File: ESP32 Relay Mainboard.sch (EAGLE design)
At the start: 88 parts, among them J2 AUDIO_JACK_TRRSSMD_RA, J3 AUDIO_JACK_TRRSSMD_RA, J4 AUDIO_JACK_TRRSSMD_RA, J5 AUDIO_JACK_TRRSSMD_RA, J6 AUDIO_JACK_TRRSSMD_RA, K1 SRD-05VDC-SL-C, K2 SRD-05VDC-SL-C, K3 SRD-05VDC-SL-C, K4 SRD-05VDC-SL-C, K5 SRD-05VDC-SL-C, K6 SRD-05VDC-SL-C, U1 ESP32-S2-WROOM, U2 CP2104, U4 LM2576SX-5.0/NOPB

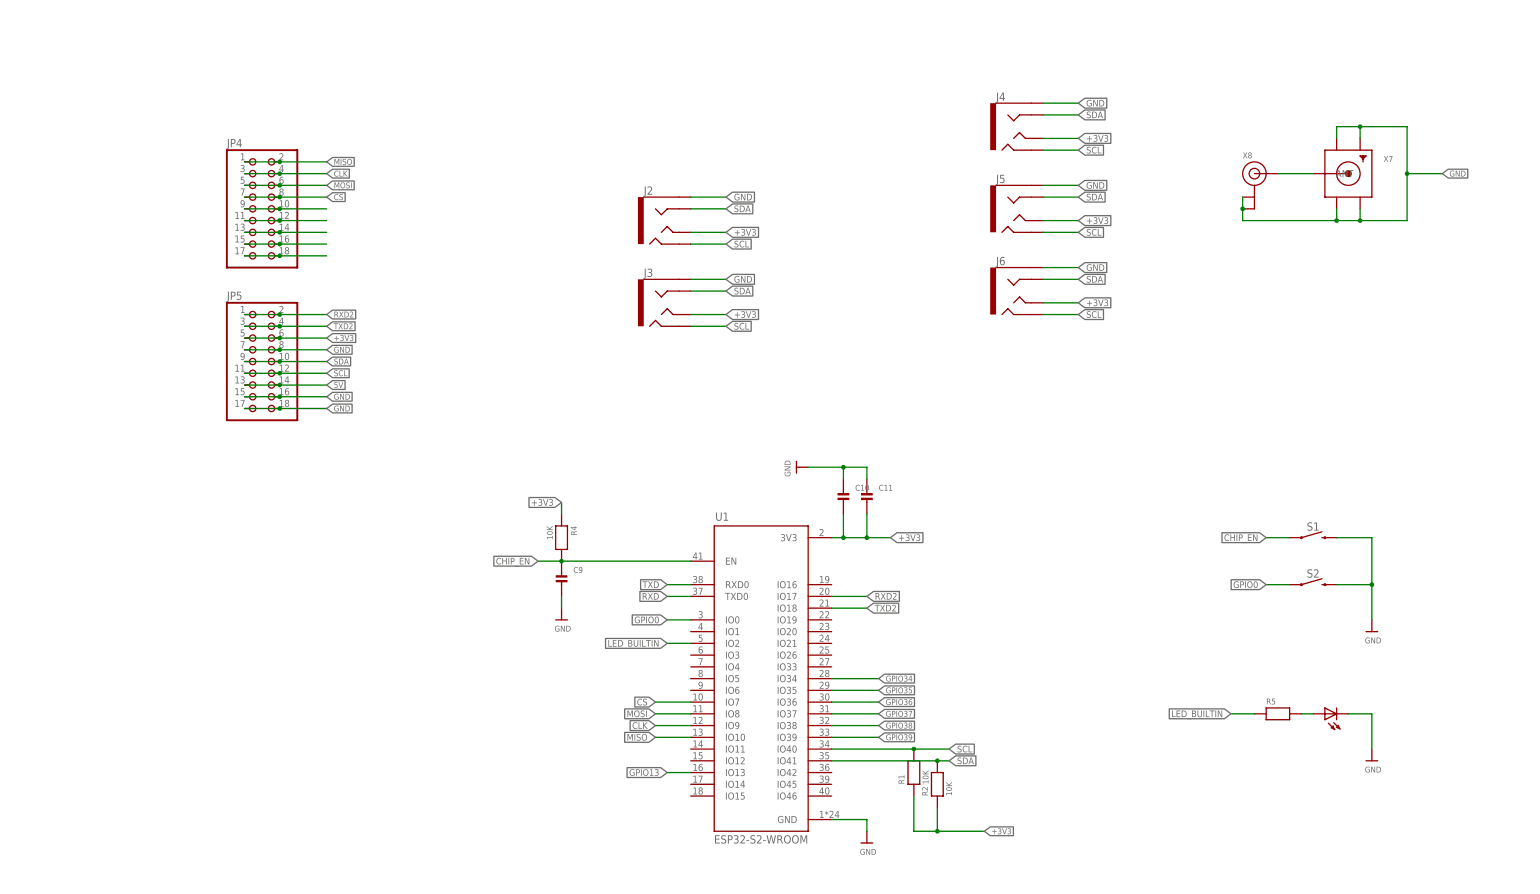
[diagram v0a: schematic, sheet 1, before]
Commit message: Add files via upload
Added second UART port. Added OTG usb. Removed CP2102. Added 6th jack connector. Added labels.
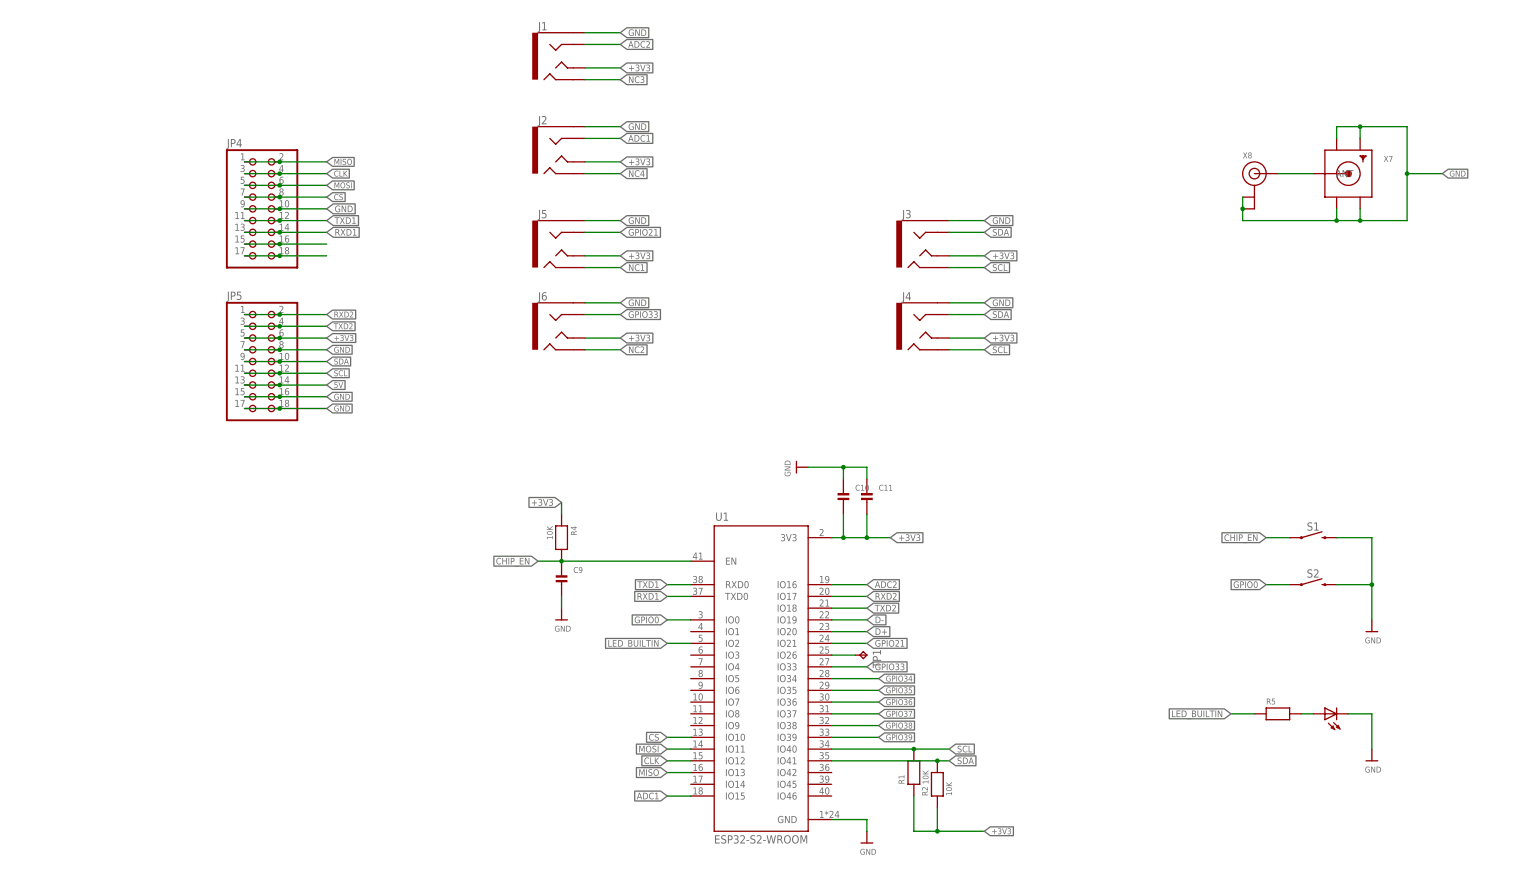
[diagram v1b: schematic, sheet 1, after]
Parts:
- removed C4: 4.7uF, SparkFun-Capacitors:22UF-0805-6.3V-20%
- removed C5: 0.1uF, SparkFun-Capacitors:22UF-0805-6.3V-20%
- removed U2: CP2104, microbuilder:CP2104
- added J1: AUDIO_JACK_TRRSSMD_RA, SparkFun-Connectors:AUDIO_JACK_TRRSSMD_RA
- added R3, R6: 5.1K, microbuilder:RESISTOR0603
- added TP1: TPTP20R, testpad:TPTP20R
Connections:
- removed net DTR: U2G$1.DTR
- removed net GPIO13: U1.IO13
- removed net N$167: JP4.10, JP4.9
- removed net N$168: JP4.11, JP4.12
- removed net N$170: JP4.13, JP4.14
- removed net RTS: U2G$1.RTS
- removed net RXD: U1.TXD0, U2G$1.RXD
- removed net TXD: U1.RXD0, U2G$1.TXD
- new net ADC1: J2.RING1, U1.IO15
- new net ADC2: J1.RING1, U1.IO16
- new net GPIO21: J5.RING1, U1.IO21
- new net GPIO33: J6.RING1, U1.IO33
- new net N$10: CONN1.CC1, R6.2
- new net N$17: TP1.TP, U1.IO26
- new net NC1: J5.RING2
- new net NC2: J6.RING2
- new net NC3: J1.RING2
- new net NC4: J2.RING2
- new net RXD1: JP4.13, JP4.14, U1.TXD0
- new net TXD1: JP4.11, JP4.12, U1.RXD0
- net +3V3: now also J1.TIP; no longer C5.1, U2G$1.REGIN, U2G$1.VDD, U2G$1.VIO
- net CLK: now also U1.IO12; no longer U1.IO9
- net CS: now also U1.IO10; no longer U1.IO7
- net D+: now also U1.IO20; no longer U2G$1.D+
- net D-: now also U1.IO19; no longer U2G$1.D-
- net GND: now also J1.EARTH, JP4.10, JP4.9, R3.1, R6.1; no longer C4.2, C5.2, U2G$1.GND, U2G$2.TP
- net MISO: now also U1.IO13; no longer U1.IO10
- net MOSI: now also U1.IO11; no longer U1.IO8
- net N$13: now also CONN1.CC2, R3.2; no longer C4.1, U2G$1.VPP
- net SCL: no longer J2.RING2, J5.RING2, J6.RING2
- net SDA: no longer J2.RING1, J5.RING1, J6.RING1
- net VBUS: no longer U2G$1.VBUS
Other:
- moved on the sheet: C1, D8, J2, J3, J4, J5, J6

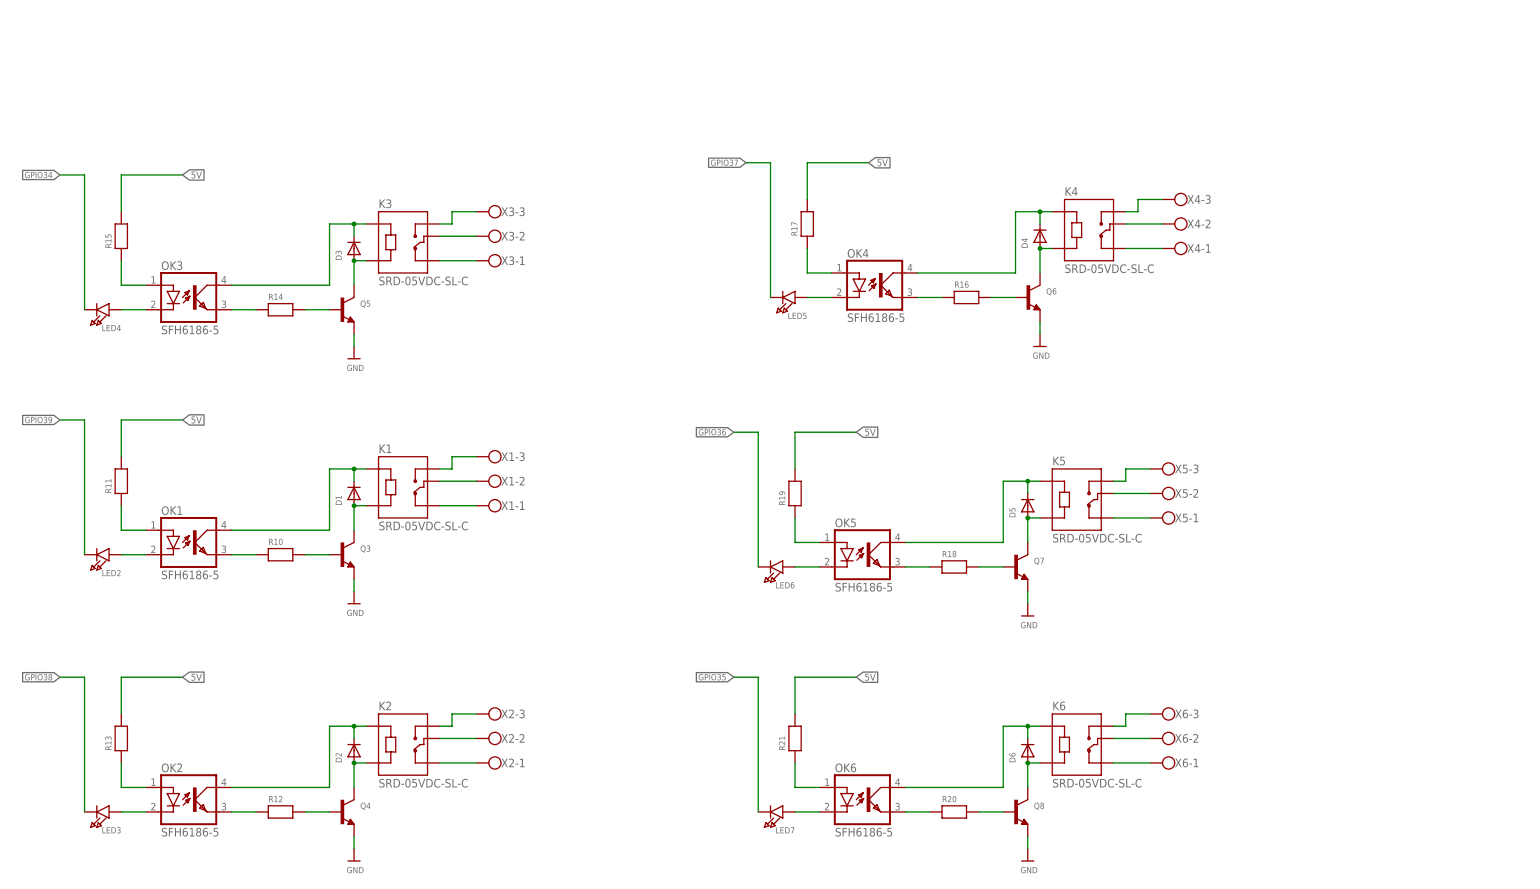
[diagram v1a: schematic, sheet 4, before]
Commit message: Updated the schematic with values
Added values to components (resistors and caps). Also added a description to some parts of the board.
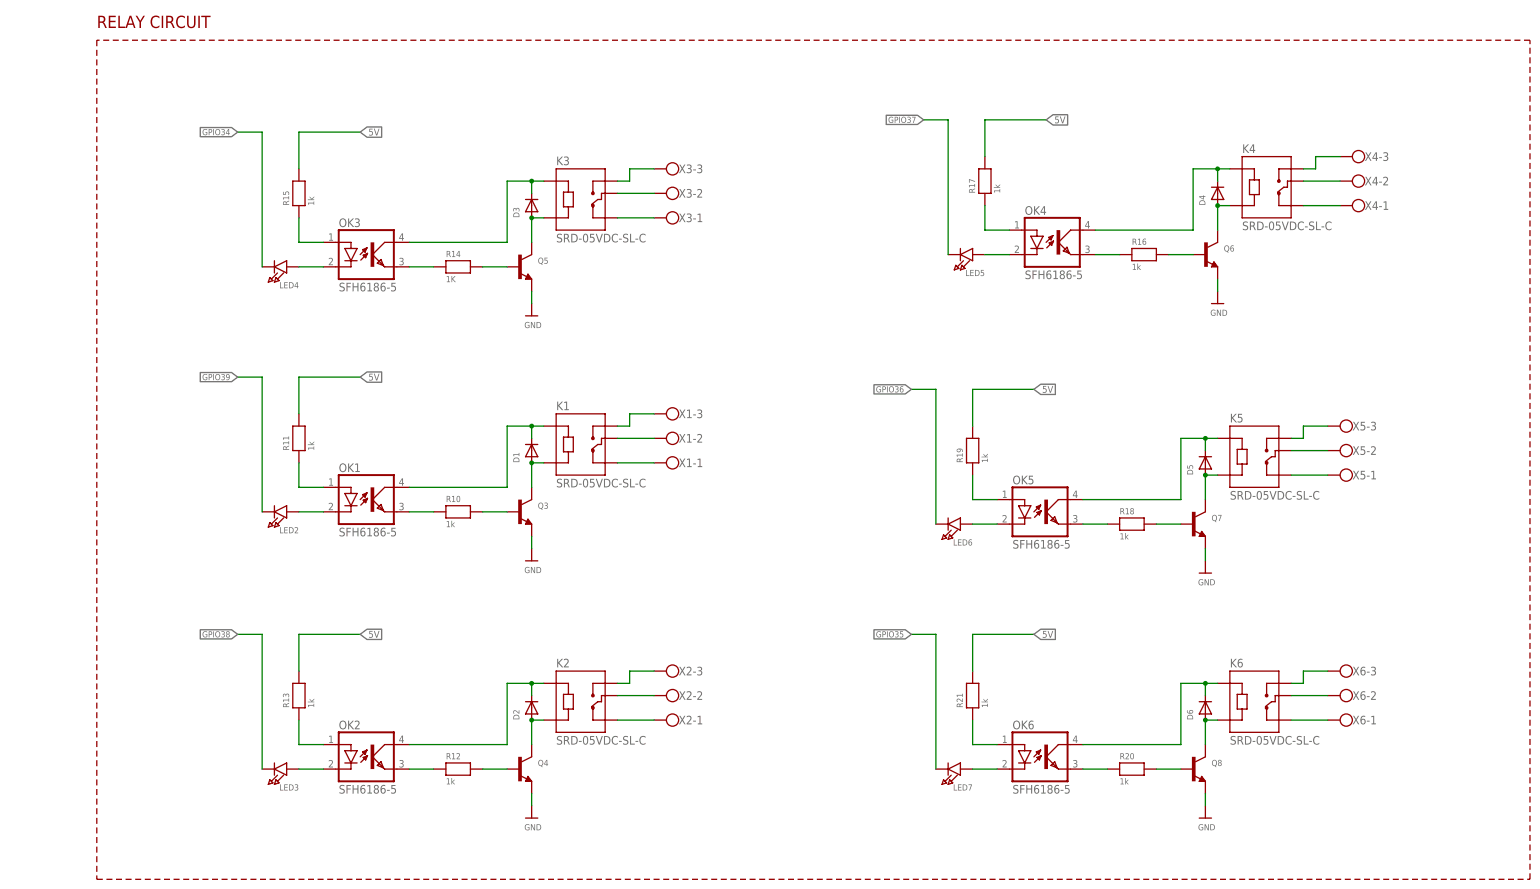
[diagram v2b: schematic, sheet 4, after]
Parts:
- C10, C9: value (none) -> 0.1uF
- C11: value (none) -> 0.1uf
- C2, C6: value (none) -> 10uF
- C3: value (none) -> 100uF
- R10, R11, R12, R13, R15, R16, R17, R18, R19, R20, R21: value (none) -> 1k
- R14, R22, R5: value (none) -> 1K
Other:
- note added: "50OHM IMPEDANCE TRACE & SMA"
- note added: "5V is directly connected to AMS1117-3.3 3.3V regulator 1A ouput"
- note added: "ANALOG JACK CONNECTORS"
- note added: "BUCK CONVERTER & REGULATOR"
- note added: "BUILTIN LED"
- note added: "Buck converter is LM2576, input is up tp 40V and output is 5V 3.5A"
- note added: "DIGITAL JACK CONNECTORS"
- note added: "ESP32-S2 MCU"
- note added: "FLASH & RESET"
- note added: "HEADER PINS"
- note added: "I2C JACK CONNECTORS"
- note added: "RELAY CIRCUIT"
- note added: "SHLD (USB-C shield pin) is left floating to avoid EMI"
- note added: "Two 5.1K resistors for USB-C connection detection."
- note added: "USB type C connector circuit with 500mA PTC fuse"
- note added: "USB-C CONNECTOR"
- note added: "reduce parasitic drain."
- note added: "to interfere in data lines. Added a 1uF capacitor to"
- moved on the sheet: C1, CONN1, D1, D2, D3, D4, D5, D6, D7, D8, F2, J1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

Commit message: Add files via upload
Removed optocouplers. added AZ1045 ESD protection array to D+ and D- lines
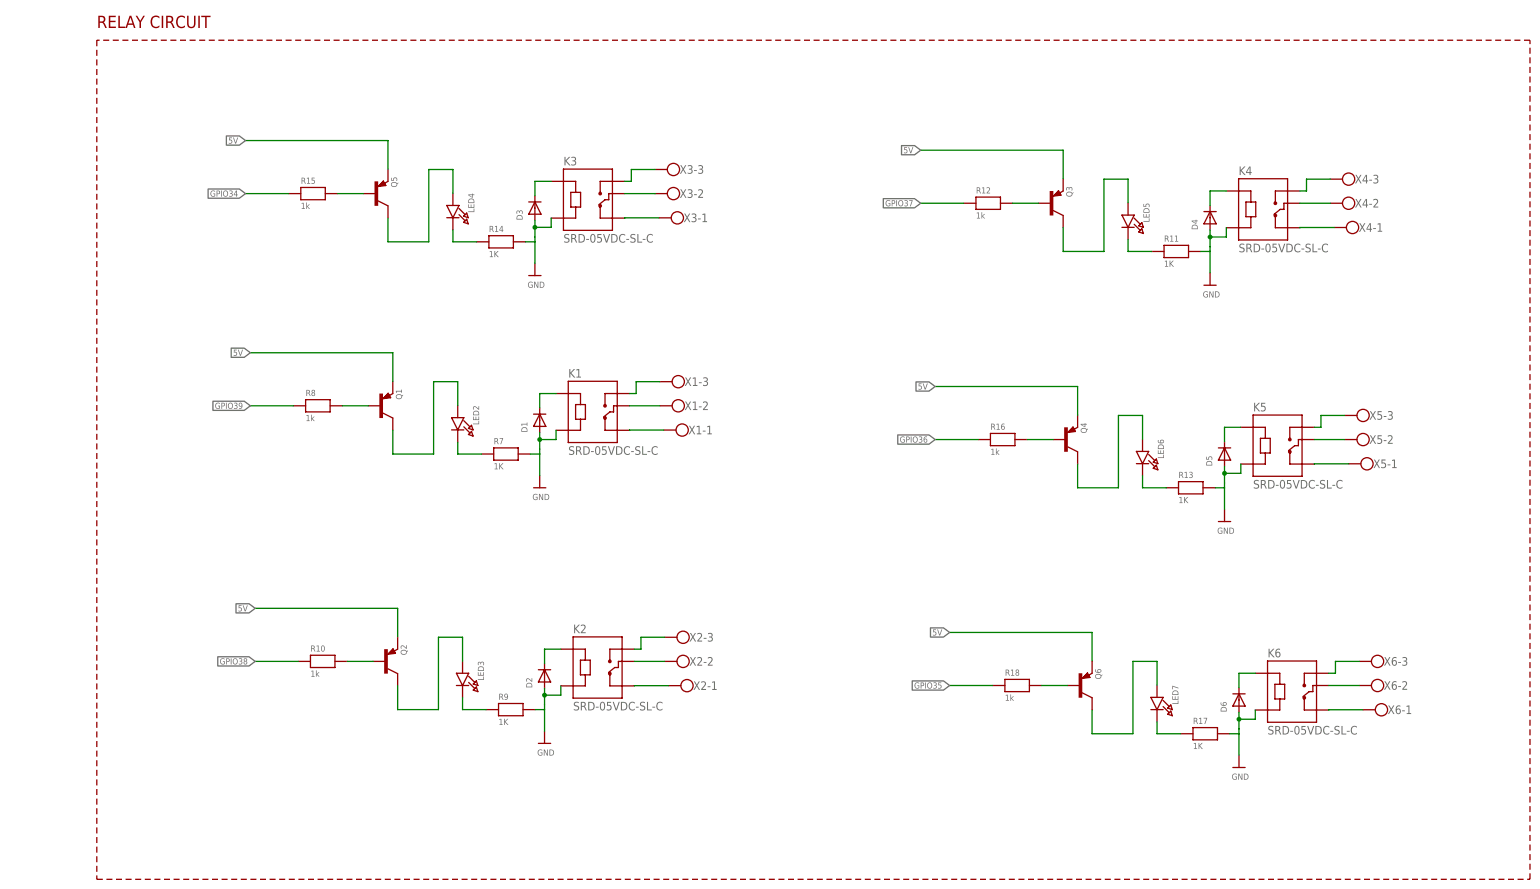
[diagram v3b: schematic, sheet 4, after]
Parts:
- removed OK1, OK2, OK3, OK4, OK5, OK6: SFH6186-5, optocoupler:SFH6186-5
- removed Q7, Q8: (no value), microbuilder:TRANSISTOR_NPN
- removed R19, R20, R21: 1k, microbuilder:RESISTOR0805
- added Q1, Q2: (no value), transistor-neu-to92:-PNP-SOT23-BCE
- added R7, R9: 1K, microbuilder:RESISTOR0805
- added R8: 1k, microbuilder:RESISTOR0805
- added U$16: AZ1045, AZ1045:AZ1045
- Q3, Q4, Q5, Q6: device microbuilder:TRANSISTOR_NPN -> transistor-neu-to92:-PNP-SOT23-BCE
- R11, R13, R17: value 1k -> 1K
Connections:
- removed net N$16 (its old number): D1.C, K1.A1, OK1.COL
- removed net N$24 (its old number): Q4.B, R12.2
- removed net N$25 (its old number): D2.A, K2.A2, Q4.C
- removed net N$26 (its old number): D2.C, K2.A1, OK2.COL
- removed net N$34 (its old number): Q5.B, R14.2
- removed net N$36 (its old number): D3.C, K3.A1, OK3.COL
- removed net N$45 (its old number): D4.A, K4.A2, Q6.C
- removed net N$46 (its old number): D4.C, K4.A1, OK4.COL
- removed net N$52 (its old number): LED6.A, OK5.C
- removed net N$53 (its old number): OK5.EMIT, R18.1
- removed net N$54: Q7.B, R18.2
- removed net N$55: D5.A, K5.A2, Q7.C
- removed net N$56: D5.C, K5.A1, OK5.COL
- removed net N$61: OK6.A, R21.1
- removed net N$62: LED7.A, OK6.C
- removed net N$63: OK6.EMIT, R20.1
- removed net N$64: Q8.B, R20.2
- removed net N$65: D6.A, K6.A2, Q8.C
- removed net N$66: D6.C, K6.A1, OK6.COL
- removed net N$9 (its old number): OK1.A, R11.1
- new net N$20: D2.C, K2.A1
- new net N$27: D3.C, K3.A1
- new net N$28: D4.C, K4.A1
- new net N$29: LED5.C, R11.1
- new net N$30: Q3.B, R12.2
- new net N$48: D6.C, K6.A1
- new net N$49: LED7.C, R17.1
- new net N$50: Q6.B, R18.2
- net 5V: now also Q1.E, Q2.E, Q3.E, Q4.E, Q5.E, Q6.E; no longer R11.2, R13.2, R15.2, R17.2, R19.2, R21.2
- net D+: now also U$16.I1, U$16.O1
- net D-: now also U$16.I2, U$16.O2
- net GND: now also D1.A, D2.A, D3.A, D4.A, D5.A, D6.A, K1.A2, K2.A2, K3.A2, K4.A2, K5.A2, K6.A2, R11.2, R13.2, R14.2, R17.2, R7.2, R9.2, U$16.GND1; no longer Q3.E, Q4.E, Q5.E, Q6.E, Q7.E, Q8.E
- net GPIO34: now also R15.1; no longer LED4.C
- net GPIO35: now also R18.1; no longer LED7.C
- net GPIO36: now also R16.1; no longer LED6.C
- net GPIO37: now also R12.1; no longer LED5.C
- net GPIO38: now also R10.1; no longer LED3.C
- net GPIO39: now also R8.1; no longer LED2.C
- net N$11: now also D1.C, K1.A1; no longer LED2.A, OK1.C
- net N$12: now also LED2.C, R7.1; no longer OK1.EMIT, R10.1
- net N$14: now also Q1.B, R8.2; no longer Q3.B, R10.2
- net N$15: now also LED2.A, Q1.C; no longer D1.A, K1.A2, Q3.C
- net N$21: now also LED3.C, R9.1; no longer OK2.A, R13.1
- net N$22: now also Q2.B, R10.2; no longer LED3.A, OK2.C
- net N$23: now also LED3.A, Q2.C; no longer OK2.EMIT, R12.1
- net N$31: now also LED4.C, R14.1; no longer OK3.A, R15.1
- net N$32: now also Q5.B, R15.2; no longer LED4.A, OK3.C
- net N$33: now also LED4.A, Q5.C; no longer OK3.EMIT, R14.1
- net N$35: now also LED5.A, Q3.C; no longer D3.A, K3.A2, Q5.C
- net N$41: now also D5.C, K5.A1; no longer OK4.A, R17.1
- net N$42: now also LED6.C, R13.1; no longer LED5.A, OK4.C
- net N$43: now also Q4.B, R16.2; no longer OK4.EMIT, R16.1
- net N$44: now also LED6.A, Q4.C; no longer Q6.B, R16.2
- net N$51: now also LED7.A, Q6.C; no longer OK5.A, R19.1
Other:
- moved on the sheet: D1, D2, D3, D4, D5, D6, K1, K2, K3, K4, K5, K6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
